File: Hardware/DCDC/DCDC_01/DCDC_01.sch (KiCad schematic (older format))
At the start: 0 parts

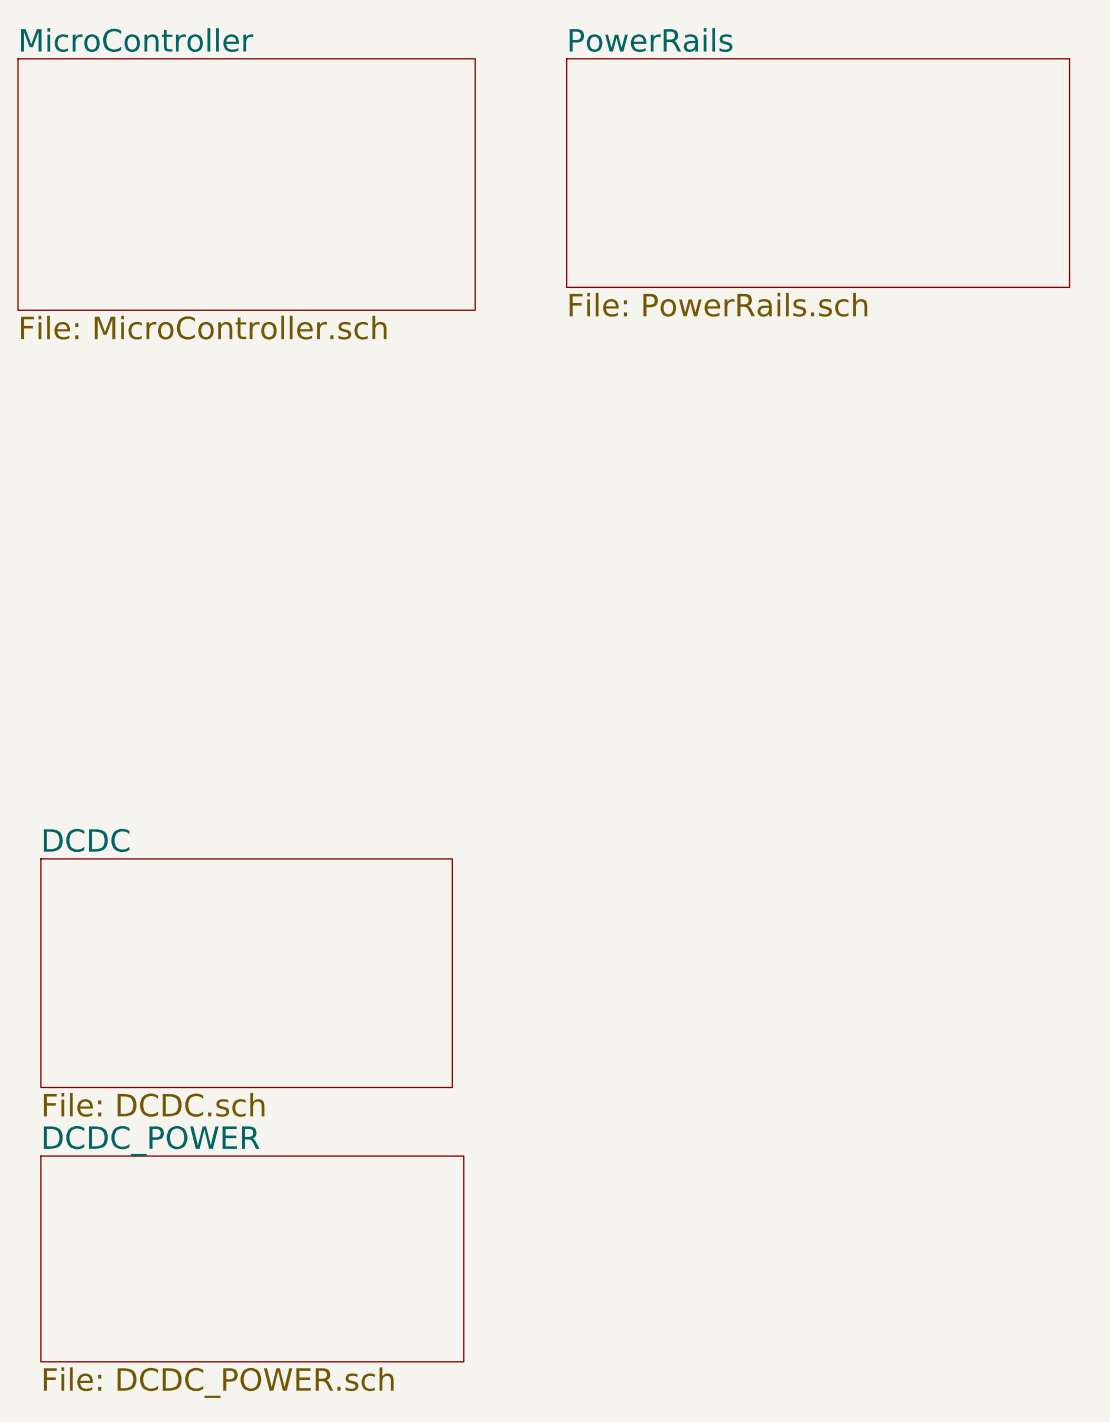
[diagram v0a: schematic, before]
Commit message: DCDC schematic update and first pass completion. Still needs review and component values
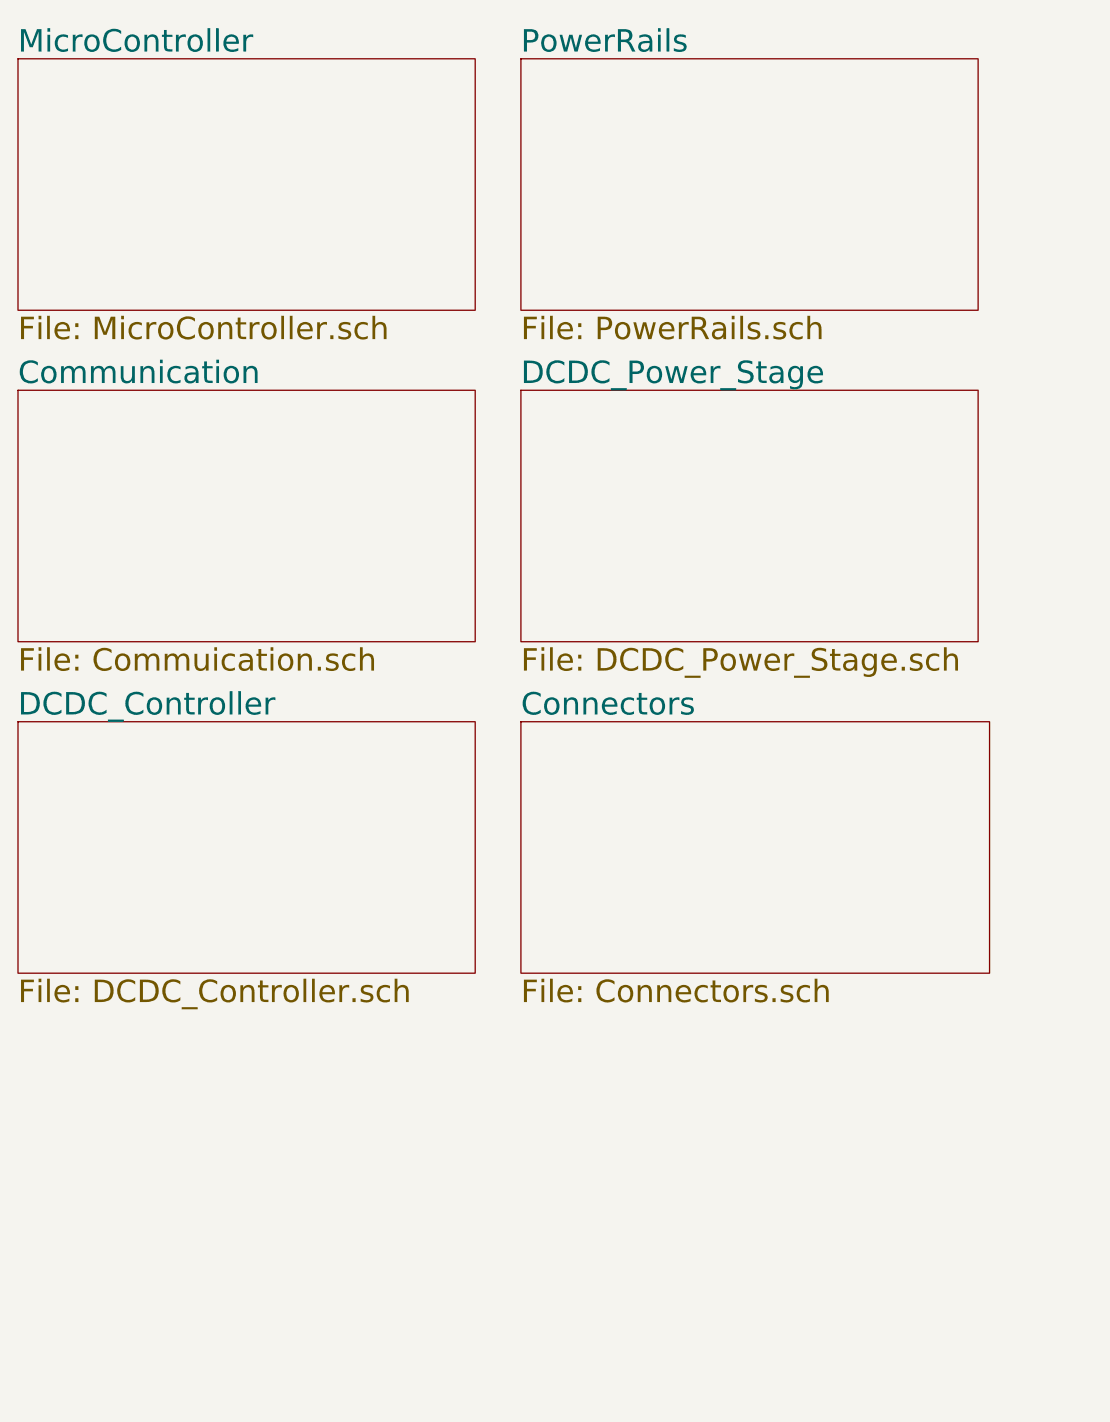
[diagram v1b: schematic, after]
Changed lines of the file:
@@
 $Descr A4 11693 8268
 encoding utf-8
-Sheet 1 5
+Sheet 1 7
 Title ""
 Date ""
@@
 $EndSheet
 $Sheet
-S 3100 700  2200 1000
+S 2900 700  2000 1100
 U 5B2FB036
 F0 "PowerRails" 98
@@
 $EndSheet
 $Sheet
-S 800  4200 1800 1000
+S 700  3600 2000 1100
 U 5B2FB0D8
-F0 "DCDC" 98
-F1 "DCDC.sch" 98
+F0 "DCDC_Controller" 98
+F1 "DCDC_Controller.sch" 98
 $EndSheet
 $Sheet
-S 800  5500 1850 900
-U 5B383331
-F0 "DCDC_POWER" 98
-F1 "DCDC_POWER.sch" 98
+S 700  2150 2000 1100
+U 5B82D31C
+F0 "Communication" 98
+F1 "Commuication.sch" 98
+$EndSheet
+$Sheet
+S 2900 2150 2000 1100
+U 5BC21A84
+F0 "DCDC_Power_Stage" 98
+F1 "DCDC_Power_Stage.sch" 98
+$EndSheet
+$Sheet
+S 2900 3600 2050 1100
+U 5C18C4A5
+F0 "Connectors" 98
+F1 "Connectors.sch" 98
 $EndSheet
 $EndSCHEMATC

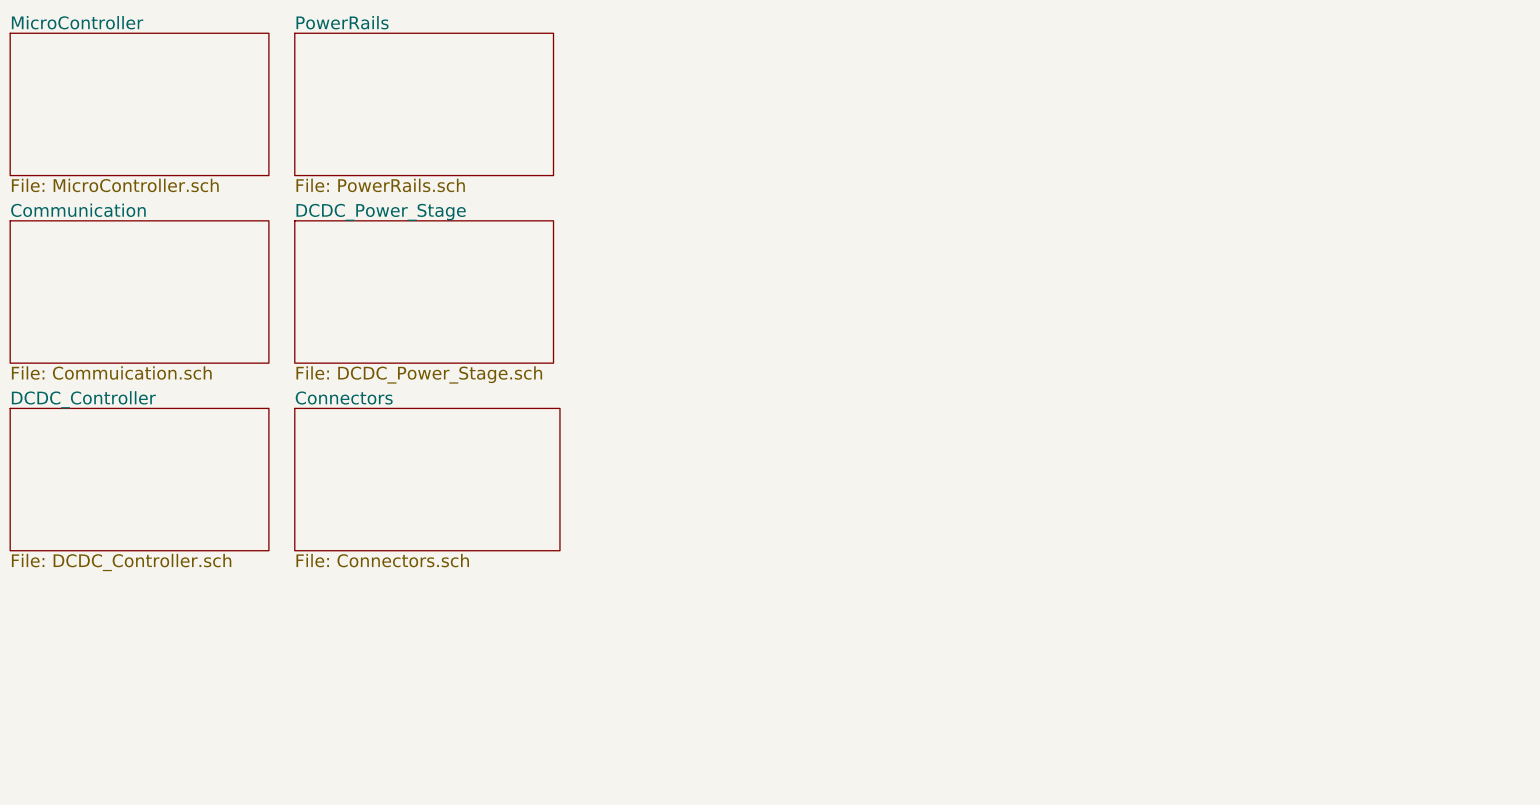
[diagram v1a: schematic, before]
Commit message: Mostly finished DCDC schematic, still needs some values and maybe a soft-start circuit that can be bypassed with 0ohm resister in case it doesn't work.
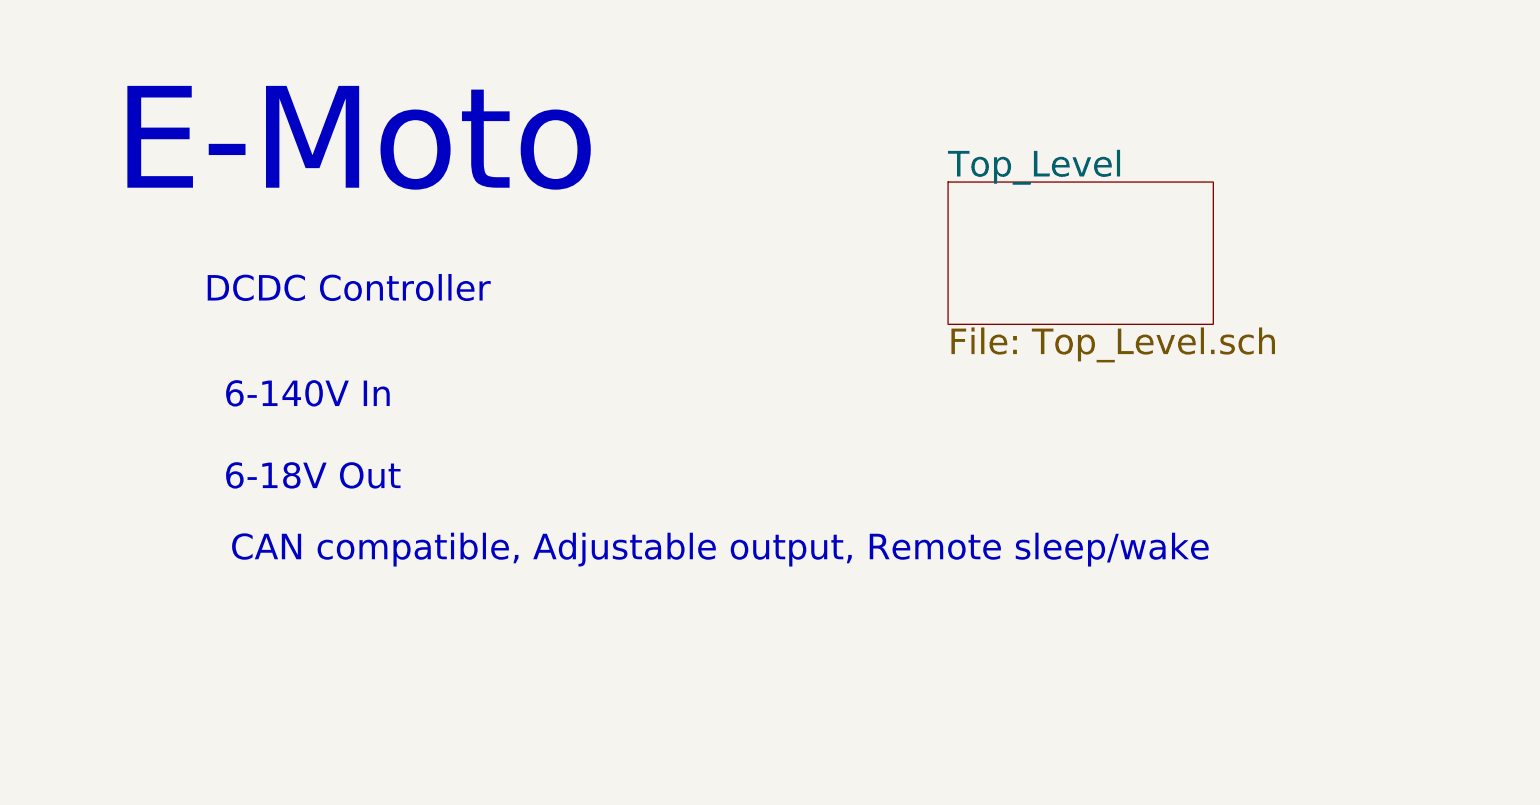
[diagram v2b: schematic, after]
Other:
- note added: "6-140V In\n\n6-18V Out"
- note added: "CAN compatible, Adjustable output, Remote sleep/wake"
- note added: "DCDC Controller"
- note added: "E-Moto"
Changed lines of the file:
@@
 $Descr A4 11693 8268
 encoding utf-8
-Sheet 1 7
+Sheet 1 8
 Title ""
 Date ""
@@
 $EndDescr
 $Sheet
-S 700  700  2000 1100
-U 5B2FAFE4
-F0 "MicroController" 98
-F1 "MicroController.sch" 98
+S 7950 1850 2050 1100
+U 5C8FC872
+F0 "Top_Level" 197
+F1 "Top_Level.sch" 197
 $EndSheet
-$Sheet
-S 2900 700  2000 1100
-U 5B2FB036
-F0 "PowerRails" 98
-F1 "PowerRails.sch" 98
-$EndSheet
-$Sheet
-S 700  3600 2000 1100
-U 5B2FB0D8
-F0 "DCDC_Controller" 98
-F1 "DCDC_Controller.sch" 98
-$EndSheet
-$Sheet
-S 700  2150 2000 1100
-U 5B82D31C
-F0 "Communication" 98
-F1 "Commuication.sch" 98
-$EndSheet
-$Sheet
-S 2900 2150 2000 1100
-U 5BC21A84
-F0 "DCDC_Power_Stage" 98
-F1 "DCDC_Power_Stage.sch" 98
-$EndSheet
-$Sheet
-S 2900 3600 2050 1100
-U 5C18C4A5
-F0 "Connectors" 98
-F1 "Connectors.sch" 98
-$EndSheet
+Text Notes 1500 2000 0    787  ~ 0
+E-Moto
+Text Notes 2200 2800 0    197  ~ 0
+DCDC Controller
+Text Notes 2350 4250 0    197  ~ 0
+6-140V In\n\n6-18V Out
+Text Notes 2400 4800 0    197  ~ 0
+CAN compatible, Adjustable output, Remote sleep/wake
 $EndSCHEMATC
